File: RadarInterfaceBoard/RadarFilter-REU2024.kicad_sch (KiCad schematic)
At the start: 35 parts, among them J1 73099-0, J2 73099-0, J2 Conn_01x04_Pin, J3 73099-0, J6 CONSMA002, J7 CONSMA002, J8 CONSMA002, J9 CONSMA002, U2 ADA4807-2ARM

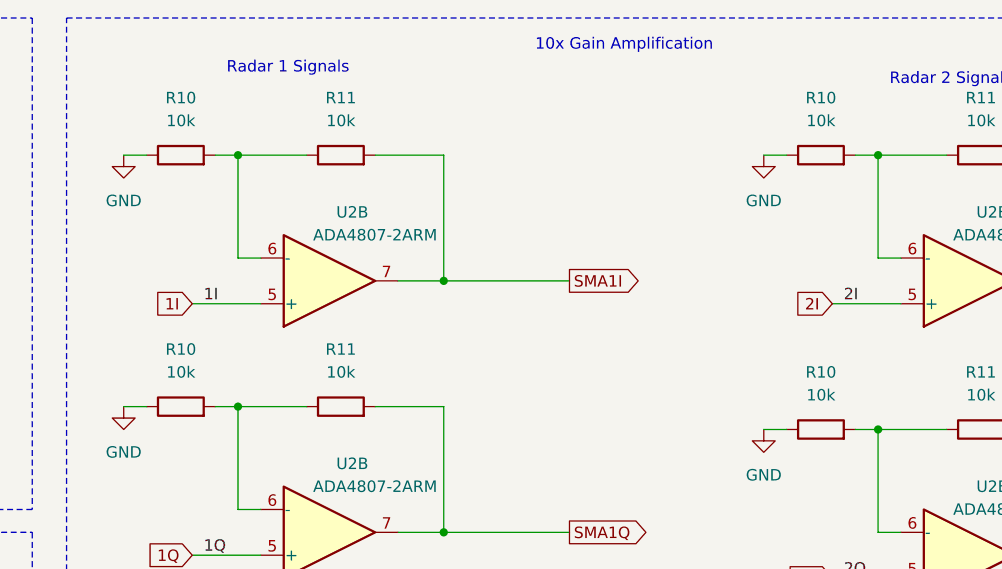
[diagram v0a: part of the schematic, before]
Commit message: fixed op-amp gain
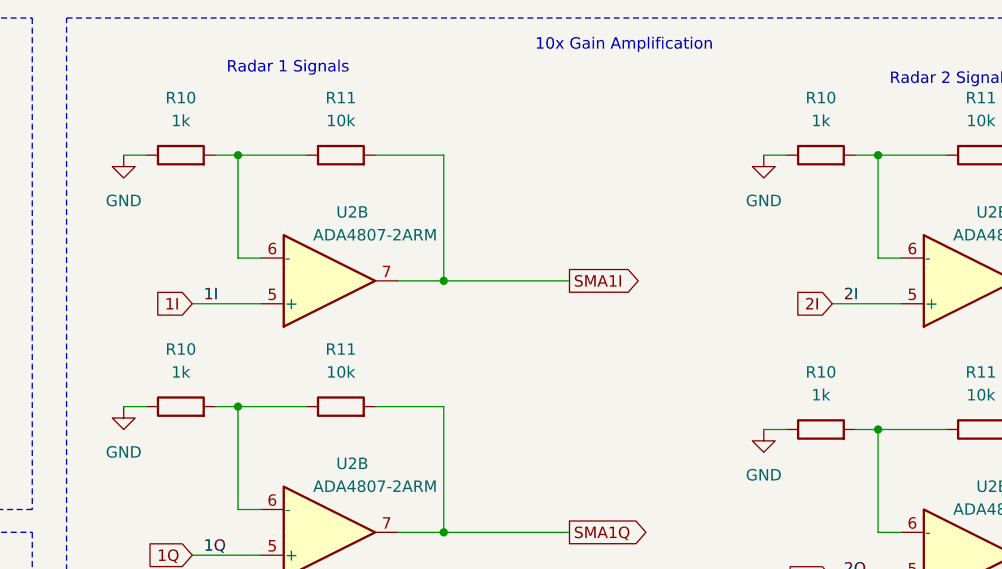
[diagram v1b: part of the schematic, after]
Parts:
- R10: value 10k -> 1k
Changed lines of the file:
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@@
       (effects (font (size 1.27 1.27)))
     )
-    (property "Value" "10k" (at 83.82 62.23 90)
+    (property "Value" "1k" (at 83.82 62.23 90)
       (effects (font (size 1.27 1.27)))
     )
@@
       (effects (font (size 1.27 1.27)))
     )
-    (property "Value" "10k" (at 83.82 34.29 90)
+    (property "Value" "1k" (at 83.82 34.29 90)
       (effects (font (size 1.27 1.27)))
     )
@@
       (effects (font (size 1.27 1.27)))
     )
-    (property "Value" "10k" (at 154.94 64.77 90)
+    (property "Value" "1k" (at 154.94 64.77 90)
       (effects (font (size 1.27 1.27)))
     )
@@
       (effects (font (size 1.27 1.27)))
     )
-    (property "Value" "10k" (at 154.94 34.29 90)
-      (effects (font (size 1.27 1.27)))
-    )
+    (property "Value" "1k" (at 154.94 34.29 90)
+      (effects (font (size 1.27 1.27)))
+    )
